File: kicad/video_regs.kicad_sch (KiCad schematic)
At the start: 4 parts, among them U140 74LS367, U147 74LS174, U148 74LS174, U149 74LS175

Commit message: More updates
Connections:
- net VRAM_{EN} renamed VMEM_{EN}
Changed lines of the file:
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@@
 	(paper "A4")
 	(bus_alias "VMODE_BUS"
-		(members "HIRES_TEXT" "GRAPHICS" "~{GRAPHICS}" "BLINK_{EN}" "VRAM_{EN}"
+		(members "HIRES_TEXT" "GRAPHICS" "~{GRAPHICS}" "BLINK_{EN}" "VMEM_{EN}"
 			"HIRES_GFX"
 		)
@@
 		)
 	)
-	(label "VRAM_{EN}"
+	(label "VMEM_{EN}"
 		(at 96.52 100.33 180)
 		(effects

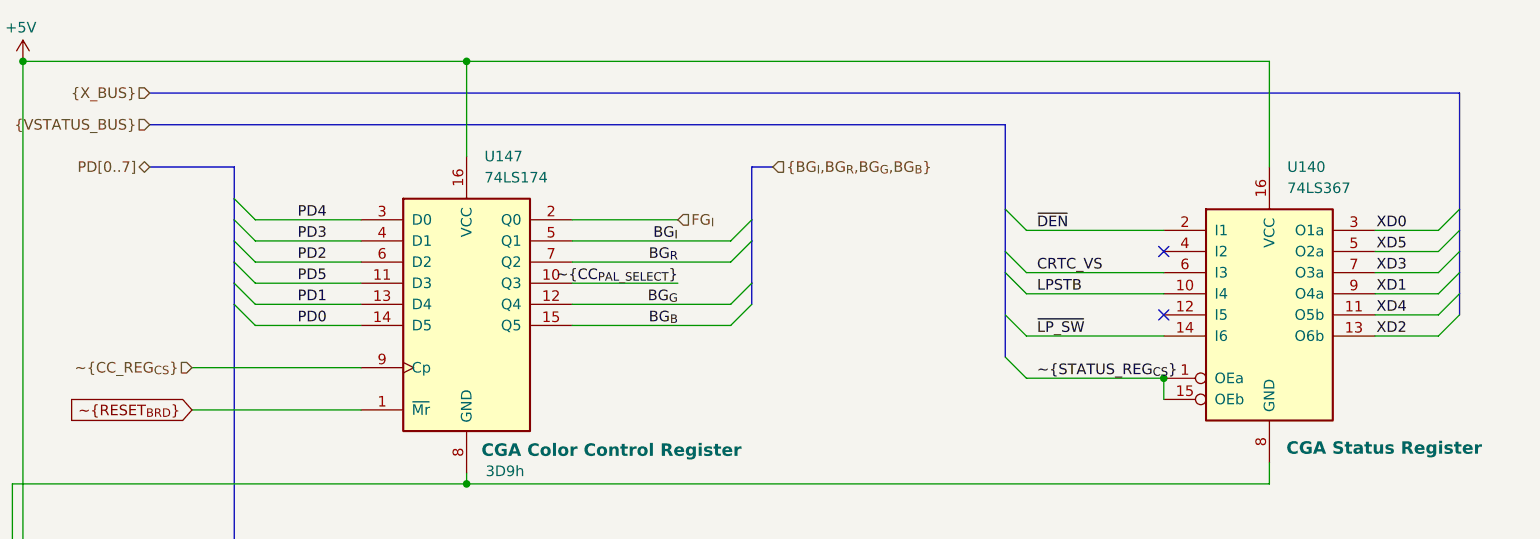
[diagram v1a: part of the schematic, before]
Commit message: Add parallel port, game port
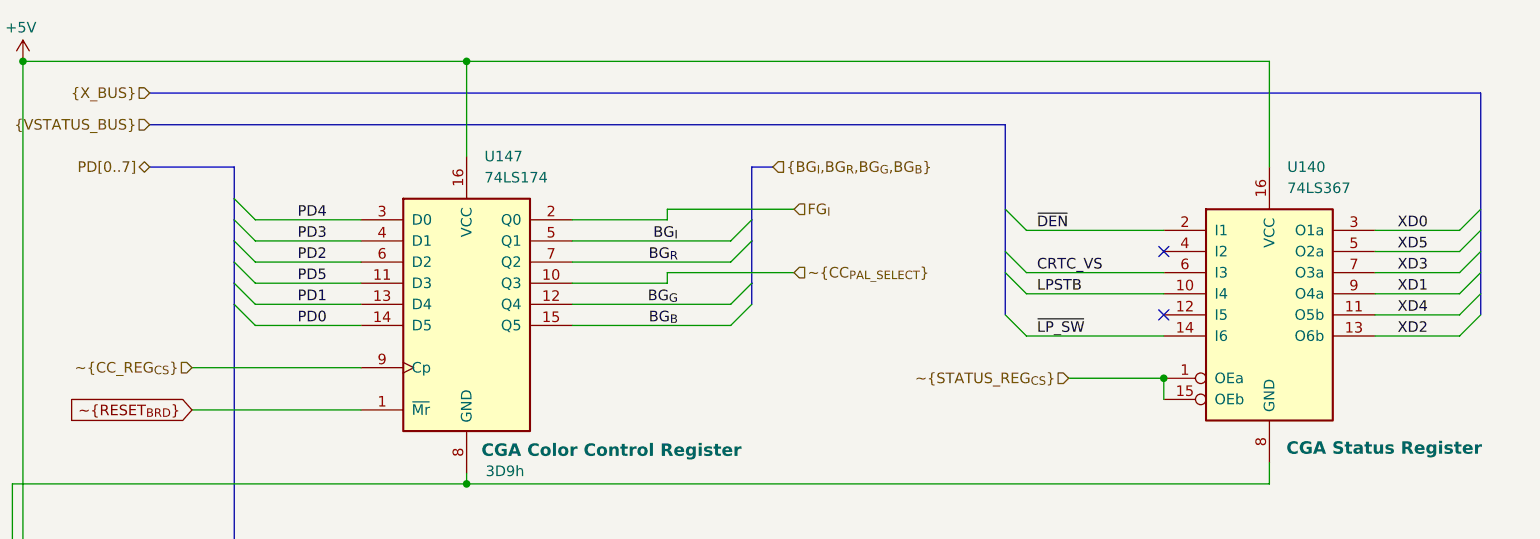
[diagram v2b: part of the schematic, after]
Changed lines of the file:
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@@
 	(bus_alias "VMODE_BUS"
 		(members "HIRES_TEXT" "GRAPHICS" "~{GRAPHICS}" "BLINK_{EN}" "VMEM_{EN}"
-			"HIRES_GFX"
+			"HIRES_GFX" "BW"
 		)
 	)
@@
 	)
 	(bus_entry
-		(at 187.96 48.26)
+		(at 190.5 48.26)
 		(size -2.54 2.54)
 		(stroke
@@
 	)
 	(bus_entry
-		(at 187.96 35.56)
+		(at 190.5 35.56)
 		(size -2.54 2.54)
 		(stroke
@@
 	)
 	(bus_entry
-		(at 133.35 53.34)
-		(size 2.54 2.54)
-		(stroke
-			(width 0)
-			(type default)
-		)
-	)
-	(bus_entry
-		(at 187.96 45.72)
+		(at 190.5 45.72)
 		(size -2.54 2.54)
 		(stroke
@@
 	)
 	(bus_entry
-		(at 187.96 40.64)
+		(at 190.5 40.64)
 		(size -2.54 2.54)
 		(stroke
@@
 	)
 	(bus_entry
-		(at 187.96 38.1)
+		(at 190.5 38.1)
 		(size -2.54 2.54)
 		(stroke
@@
 	)
 	(bus_entry
-		(at 187.96 43.18)
+		(at 190.5 43.18)
 		(size -2.54 2.54)
 		(stroke
@@
 		)
 	)
+	(wire
+		(pts
+			(xy 177.8 43.18) (xy 187.96 43.18)
+		)
+		(stroke
+			(width 0)
+			(type default)
+		)
+	)
 	(bus
 		(pts
@@
 	(wire
 		(pts
+			(xy 177.8 38.1) (xy 187.96 38.1)
+		)
+		(stroke
+			(width 0)
+			(type default)
+		)
+	)
+	(wire
+		(pts
 			(xy 55.88 100.33) (xy 43.18 100.33)
 		)
@@
 	(wire
 		(pts
+			(xy 177.8 48.26) (xy 187.96 48.26)
+		)
+		(stroke
+			(width 0)
+			(type default)
+		)
+	)
+	(wire
+		(pts
 			(xy 55.88 49.53) (xy 43.18 49.53)
 		)
@@
 	(wire
 		(pts
-			(xy 135.89 55.88) (xy 152.4 55.88)
+			(xy 140.97 55.88) (xy 152.4 55.88)
 		)
 		(stroke
@@
 	(wire
 		(pts
-			(xy 81.28 44.45) (xy 93.98 44.45)
-		)
-		(stroke
-			(width 0)
-			(type default)
-		)
-	)
-	(bus
-		(pts
-			(xy 187.96 43.18) (xy 187.96 45.72)
+			(xy 92.71 43.18) (xy 107.95 43.18)
+		)
+		(stroke
+			(width 0)
+			(type default)
+		)
+	)
+	(wire
+		(pts
+			(xy 92.71 43.18) (xy 92.71 44.45)
+		)
+		(stroke
+			(width 0)
+			(type default)
+		)
+	)
+	(bus
+		(pts
+			(xy 190.5 43.18) (xy 190.5 45.72)
 		)
 		(stroke
@@
 		)
 	)
-	(wire
-		(pts
-			(xy 185.42 48.26) (xy 177.8 48.26)
-		)
-		(stroke
-			(width 0)
-			(type default)
-		)
-	)
-	(bus
-		(pts
-			(xy 187.96 40.64) (xy 187.96 43.18)
+	(bus
+		(pts
+			(xy 190.5 40.64) (xy 190.5 43.18)
 		)
 		(stroke
@@
 		)
 	)
+	(wire
+		(pts
+			(xy 92.71 44.45) (xy 81.28 44.45)
+		)
+		(stroke
+			(width 0)
+			(type default)
+		)
+	)
 	(bus
 		(pts
@@
 	(wire
 		(pts
-			(xy 185.42 45.72) (xy 177.8 45.72)
+			(xy 177.8 50.8) (xy 187.96 50.8)
 		)
 		(stroke
@@
 		)
 	)
-	(wire
-		(pts
-			(xy 185.42 50.8) (xy 177.8 50.8)
-		)
-		(stroke
-			(width 0)
-			(type default)
-		)
-	)
-	(bus
-		(pts
-			(xy 187.96 38.1) (xy 187.96 40.64)
+	(bus
+		(pts
+			(xy 190.5 38.1) (xy 190.5 40.64)
 		)
 		(stroke
@@
 	(wire
 		(pts
-			(xy 185.42 43.18) (xy 177.8 43.18)
-		)
-		(stroke
-			(width 0)
-			(type default)
-		)
-	)
-	(wire
-		(pts
 			(xy 68.58 123.19) (xy 13.97 123.19)
 		)
@@
 	(wire
 		(pts
+			(xy 177.8 45.72) (xy 187.96 45.72)
+		)
+		(stroke
+			(width 0)
+			(type default)
+		)
+	)
+	(wire
+		(pts
 			(xy 165.1 17.78) (xy 165.1 30.48)
 		)
@@
 	(bus
 		(pts
-			(xy 187.96 45.72) (xy 187.96 48.26)
+			(xy 190.5 45.72) (xy 190.5 48.26)
 		)
 		(stroke
@@
 		)
 	)
-	(bus
-		(pts
-			(xy 133.35 48.26) (xy 133.35 53.34)
-		)
-		(stroke
-			(width 0)
-			(type default)
-		)
-	)
 	(wire
 		(pts
@@
 	(wire
 		(pts
-			(xy 185.42 38.1) (xy 177.8 38.1)
-		)
-		(stroke
-			(width 0)
-			(type default)
-		)
-	)
-	(wire
-		(pts
 			(xy 43.18 147.32) (xy 54.61 147.32)
 		)
@@
 	(bus
 		(pts
-			(xy 30.48 21.59) (xy 187.96 21.59)
+			(xy 30.48 21.59) (xy 190.5 21.59)
 		)
 		(stroke
@@
 	(wire
 		(pts
+			(xy 177.8 40.64) (xy 187.96 40.64)
+		)
+		(stroke
+			(width 0)
+			(type default)
+		)
+	)
+	(wire
+		(pts
 			(xy 67.31 179.07) (xy 67.31 177.8)
 		)
@@
 	(bus
 		(pts
-			(xy 187.96 21.59) (xy 187.96 35.56)
+			(xy 190.5 21.59) (xy 190.5 35.56)
 		)
 		(stroke
@@
 		)
 	)
+	(wire
+		(pts
+			(xy 92.71 36.83) (xy 81.28 36.83)
+		)
+		(stroke
+			(width 0)
+			(type default)
+		)
+	)
 	(bus
 		(pts
@@
 	(wire
 		(pts
-			(xy 81.28 36.83) (xy 93.98 36.83)
+			(xy 92.71 35.56) (xy 107.95 35.56)
 		)
 		(stroke
@@
 		)
 	)
-	(wire
-		(pts
-			(xy 185.42 40.64) (xy 177.8 40.64)
-		)
-		(stroke
-			(width 0)
-			(type default)
-		)
-	)
 	(bus
 		(pts
@@
 	(wire
 		(pts
+			(xy 92.71 35.56) (xy 92.71 36.83)
+		)
+		(stroke
+			(width 0)
+			(type default)
+		)
+	)
+	(wire
+		(pts
 			(xy 67.31 137.16) (xy 67.31 139.7)
 		)
@@
 	(bus
 		(pts
-			(xy 187.96 35.56) (xy 187.96 38.1)
+			(xy 190.5 35.56) (xy 190.5 38.1)
 		)
 		(stroke
@@
 	)
 	(label "XD0"
-		(at 181.61 38.1 180)
-		(effects
-			(font
-				(size 1.27 1.27)
-			)
-			(justify right bottom)
-		)
-	)
-	(label "~{CC_{PAL_SELECT}}"
-		(at 93.98 44.45 180)
+		(at 184.15 38.1 180)
 		(effects
 			(font
@@
 	)
 	(label "XD3"
-		(at 181.61 43.18 180)
+		(at 184.15 43.18 180)
 		(effects
 			(font
@@
 	)
 	(label "XD4"
-		(at 181.61 48.26 180)
+		(at 184.15 48.26 180)
 		(effects
 			(font
@@
 	)
 	(label "XD1"
-		(at 181.61 45.72 180)
+		(at 184.15 45.72 180)
 		(effects
 			(font
@@
 		)
 	)
-	(label "~{STATUS_REG_{CS}}"
-		(at 137.16 55.88 0)
-		(effects
-			(font
-				(size 1.27 1.27)
-			)
-			(justify left bottom)
-		)
-	)
 	(label "PD3"
 		(at 46.99 162.56 0)
@@
 	)
 	(label "XD5"
-		(at 181.61 40.64 180)
+		(at 184.15 40.64 180)
 		(effects
 			(font
@@
 	)
 	(label "XD2"
-		(at 181.61 50.8 180)
+		(at 184.15 50.8 180)
 		(effects
 			(font
@@
 	(hierarchical_label "FG_{I}"
 		(shape input)
-		(at 93.98 36.83 0)
+		(at 107.95 35.56 0)
 		(effects
 			(font
@@
 		)
 	)
+	(hierarchical_label "~{CC_{PAL_SELECT}}"
+		(shape input)
+		(at 107.95 43.18 0)
+		(effects
+			(font
+				(size 1.27 1.27)
+			)
+			(justify left)
+		)
+	)
 	(hierarchical_label "~{OPTION_REG_3_{CS}}"
 		(shape input)
@@
 		(effects
 			(font
+				(size 1.27 1.27)
+			)
+			(justify right)
+		)
+	)
+	(hierarchical_label "~{STATUS_REG_{CS}}"
+		(shape input)
+		(at 140.97 55.88 180)
+		(effects
+			(font
